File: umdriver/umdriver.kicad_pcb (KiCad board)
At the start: 4 copper layers, 117.6 x 100 mm, 87 parts, among them J1 SWD, J10 Conn_01x01, J2 Conn_01x08, J3 Isolated rs485, J4 Conn_01x01, J5 Conn_01x01, J6 Conn_01x01, J7 Conn_01x01, J8 Conn_01x01, J9 Conn_01x01, K1 SPST, Q1 Q_NMOS_GDS, SW1 SW_Reset, SW2 SW_Test, U1 STGIPQ8C60T, U2 NCP718, U3 ATSAMD21G18A-AUT, U4 ISO3088DW, Y1 32.768

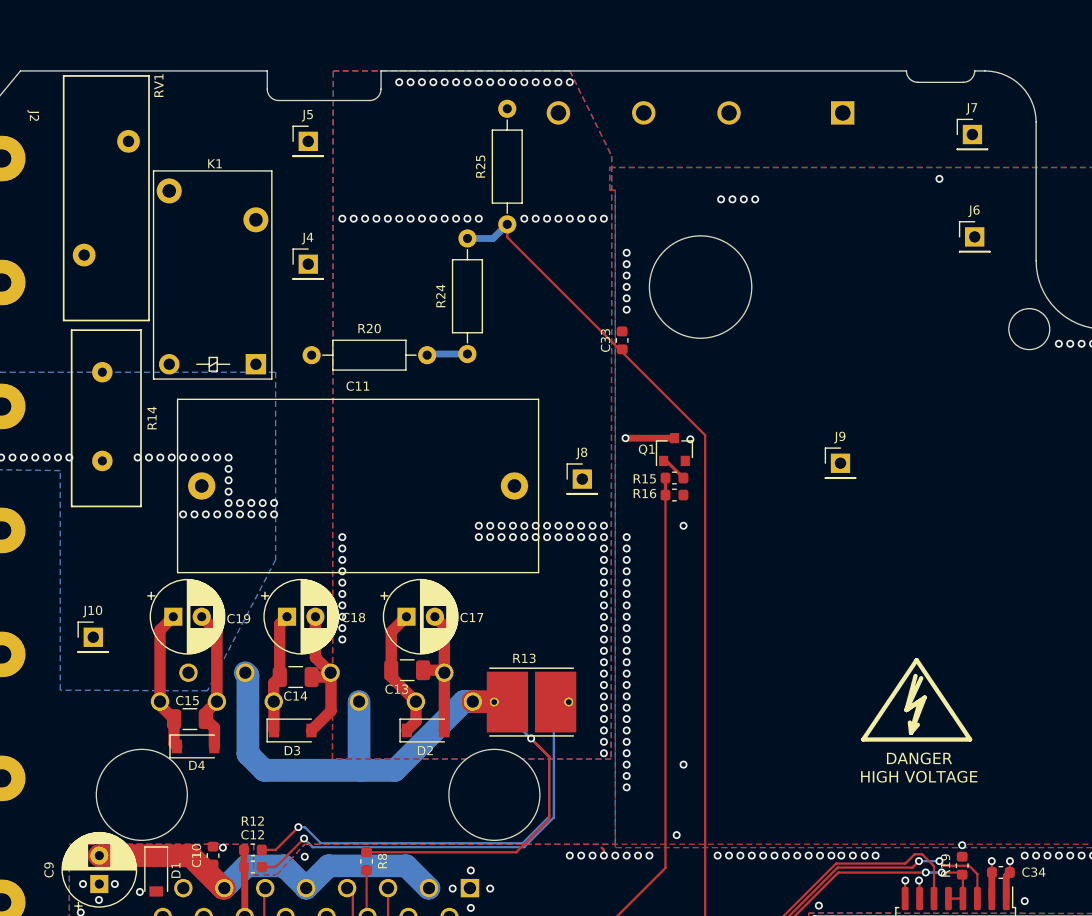
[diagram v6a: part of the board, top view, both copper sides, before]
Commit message: Add DC BUS board connectors, move stuff a bit, fix VOUT zone so it's capable to thruput some current
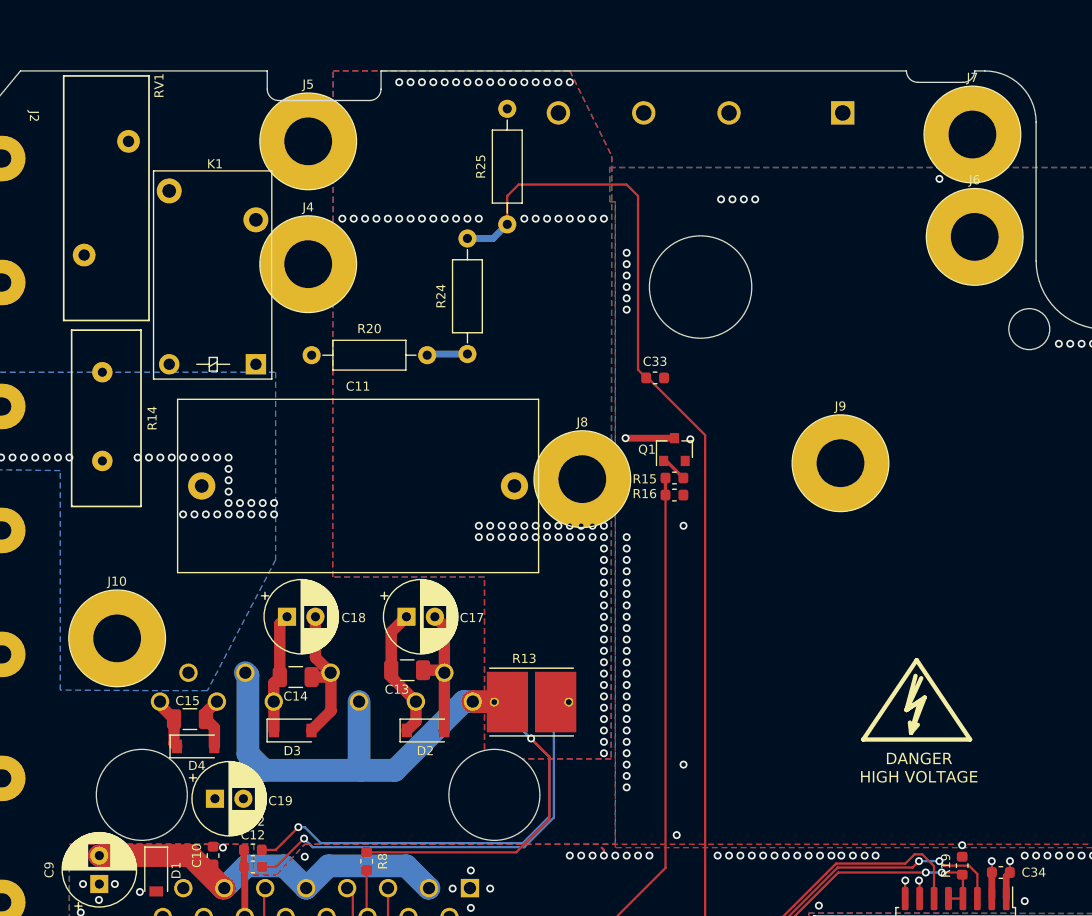
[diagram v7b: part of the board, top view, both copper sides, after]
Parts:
- J10, J4, J5, J6, J7, J8, J9: footprint Pin_Headers:Pin_Header_Straight_1x01_Pitch2.54mm -> umdriver:WURTH-7466003
- moved C19 16.4 mm to (81.8, 104.0)
- moved C33 4.39 mm to (120.5, 67.0), turned to 0 degrees
- moved J10 2.10 mm to (73.2, 89.9)
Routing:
- net /DC_BUS_MON: track 111.5 -> 124.0 mm
- net /UOUT: track 12.7 -> 4.65 mm
- net /VBOOTU: track 12.5 -> 4.55 mm
- net GND: vias 273 -> 263
